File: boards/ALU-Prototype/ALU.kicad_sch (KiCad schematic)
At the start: 10 parts

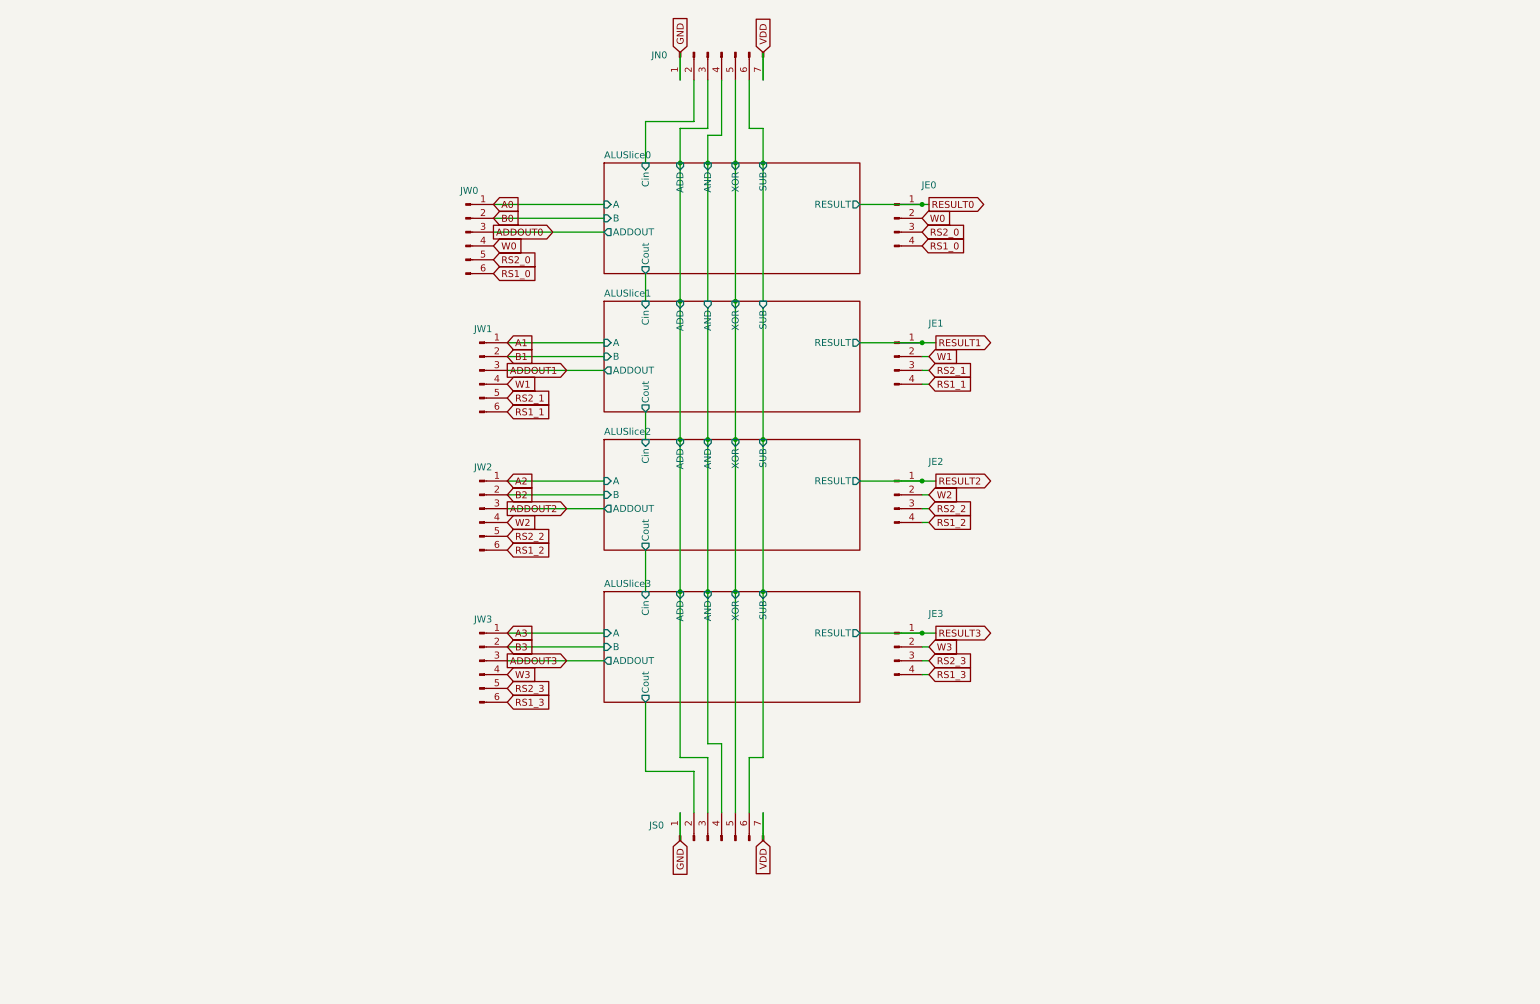
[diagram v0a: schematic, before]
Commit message: pin headers (2*17 and 2*8)
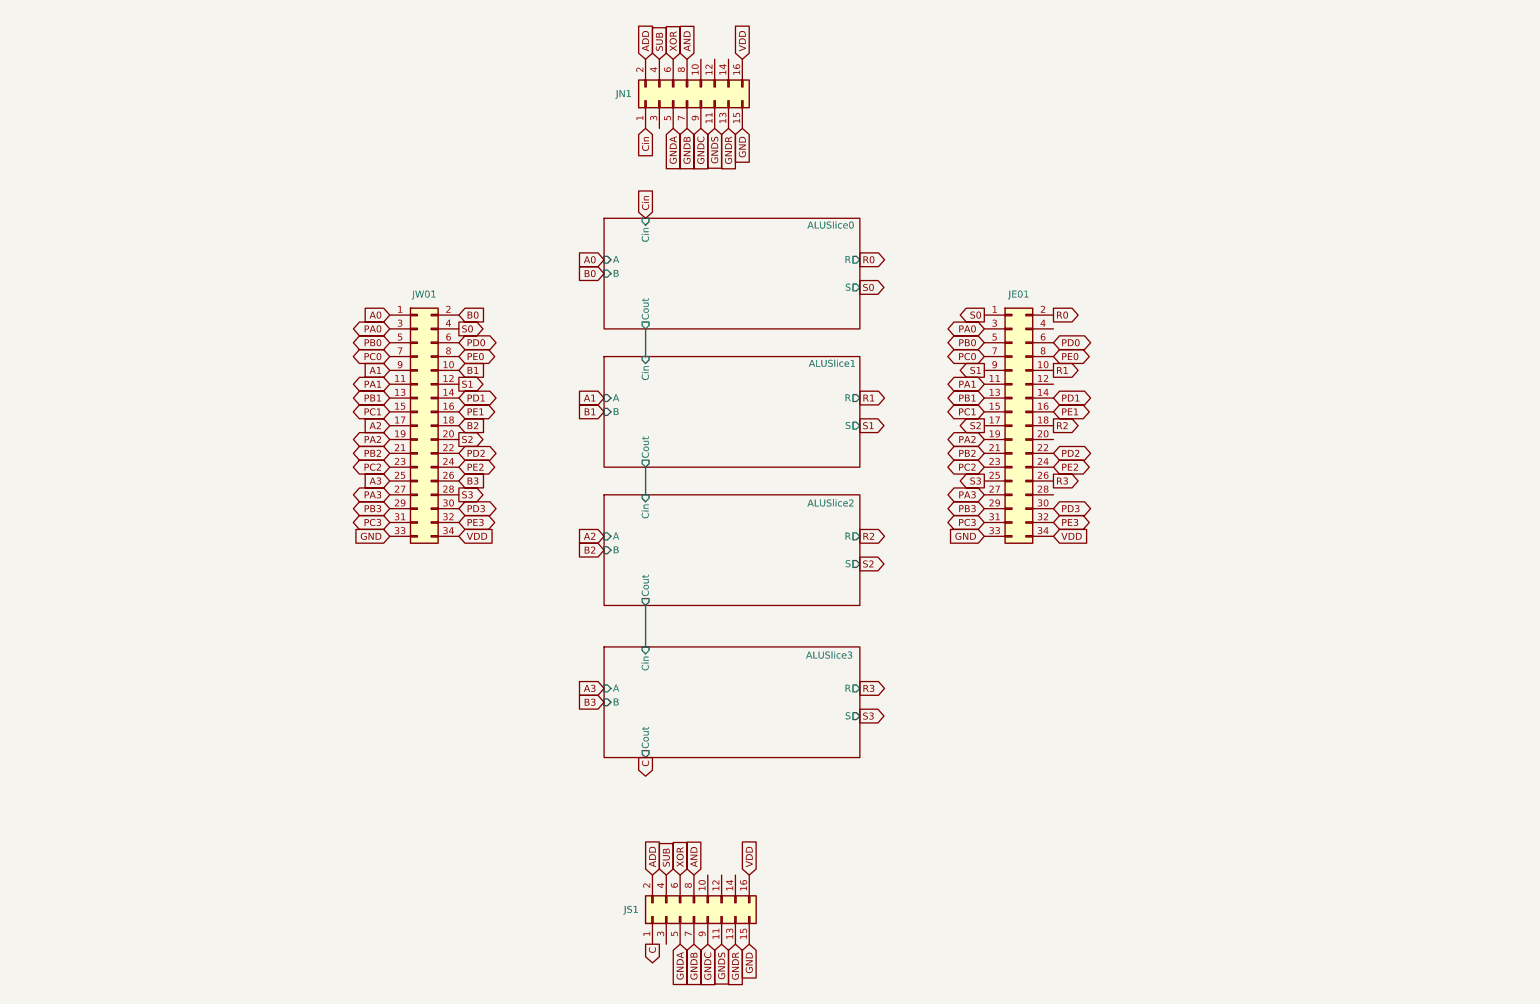
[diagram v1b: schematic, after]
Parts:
- removed JE0, JE1, JE2, JE3: Conn_01x04_Pin, Connector_PinHeader_1.27mm:PinHeader_1x04_P1.27mm_Vertical, symbol Connector:Conn_01x04_Pin
- removed JN0, JS0: Conn_01x07_Pin, Connector_PinHeader_1.27mm:PinHeader_1x07_P1.27mm_Vertical, symbol Connector:Conn_01x07_Pin
- removed JW0, JW1, JW2, JW3: Conn_01x06_Pin, Connector_PinHeader_1.27mm:PinHeader_1x06_P1.27mm_Vertical, symbol Connector:Conn_01x06_Pin
- added JE01, JW01: Conn_02x17_Odd_Even, Connector_PinHeader_2.54mm:PinHeader_2x17_P2.54mm_Vertical, symbol Connector_Generic:Conn_02x17_Odd_Even
- added JN1, JS1: Conn_02x08_Odd_Even, Connector_PinHeader_2.54mm:PinHeader_2x08_P2.54mm_Vertical, symbol Connector_Generic:Conn_02x08_Odd_Even
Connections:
- net A0: now also JW01.1 (Pin_1)
- net A1: now also JW01.9 (Pin_9)
- net A2: now also JW01.17 (Pin_17)
- net A3: now also JW01.25 (Pin_25)
- net B0: now also JW01.2 (Pin_2)
- net B1: now also JW01.10 (Pin_10)
- net B2: now also JW01.18 (Pin_18)
- net B3: now also JW01.26 (Pin_26)
- net GND: now also JE01.33 (Pin_33), JN1.15 (Pin_15), JS1.15 (Pin_15), JW01.33 (Pin_33)
- net VDD: now also JE01.34 (Pin_34), JN1.16 (Pin_16), JS1.16 (Pin_16), JW01.34 (Pin_34)
- new net ADD: JN1.2 (Pin_2), JS1.2 (Pin_2)
- new net AND: JN1.8 (Pin_8), JS1.8 (Pin_8)
- new net C: JS1.1 (Pin_1)
- new net Cin: JN1.1 (Pin_1)
- new net GNDA: JN1.5 (Pin_5), JS1.5 (Pin_5)
- new net GNDB: JN1.7 (Pin_7), JS1.7 (Pin_7)
- new net GNDC: JN1.9 (Pin_9), JS1.9 (Pin_9)
- new net GNDR: JN1.13 (Pin_13), JS1.13 (Pin_13)
- new net GNDS: JN1.11 (Pin_11), JS1.11 (Pin_11)
- new net PA0: JE01.3 (Pin_3), JW01.3 (Pin_3)
- new net PA1: JE01.11 (Pin_11), JW01.11 (Pin_11)
- new net PA2: JE01.19 (Pin_19), JW01.19 (Pin_19)
- new net PA3: JE01.27 (Pin_27), JW01.27 (Pin_27)
- new net PB0: JE01.5 (Pin_5), JW01.5 (Pin_5)
- new net PB1: JE01.13 (Pin_13), JW01.13 (Pin_13)
- new net PB2: JE01.21 (Pin_21), JW01.21 (Pin_21)
- new net PB3: JE01.29 (Pin_29), JW01.29 (Pin_29)
- new net PC0: JE01.7 (Pin_7), JW01.7 (Pin_7)
- new net PC1: JE01.15 (Pin_15), JW01.15 (Pin_15)
- new net PC2: JE01.23 (Pin_23), JW01.23 (Pin_23)
- new net PC3: JE01.31 (Pin_31), JW01.31 (Pin_31)
- new net PD0: JE01.6 (Pin_6), JW01.6 (Pin_6)
- new net PD1: JE01.14 (Pin_14), JW01.14 (Pin_14)
- new net PD2: JE01.22 (Pin_22), JW01.22 (Pin_22)
- new net PD3: JE01.30 (Pin_30), JW01.30 (Pin_30)
- new net PE0: JE01.8 (Pin_8), JW01.8 (Pin_8)
- new net PE1: JE01.16 (Pin_16), JW01.16 (Pin_16)
- new net PE2: JE01.24 (Pin_24), JW01.24 (Pin_24)
- new net PE3: JE01.32 (Pin_32), JW01.32 (Pin_32)
- new net R0: JE01.2 (Pin_2)
- new net R1: JE01.10 (Pin_10)
- new net R2: JE01.18 (Pin_18)
- new net R3: JE01.26 (Pin_26)
- new net S0: JE01.1 (Pin_1), JW01.4 (Pin_4)
- new net S1: JE01.9 (Pin_9), JW01.12 (Pin_12)
- new net S2: JE01.17 (Pin_17), JW01.20 (Pin_20)
- new net S3: JE01.25 (Pin_25), JW01.28 (Pin_28)
- new net SUB: JN1.4 (Pin_4), JS1.4 (Pin_4)
- new net XOR: JN1.6 (Pin_6), JS1.6 (Pin_6)
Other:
- sheet ALUSlice0 ports: added R, S; removed ADD, ADDOUT, AND, RESULT, SUB, XOR
- sheet ALUSlice1 ports: added R, S; removed ADD, ADDOUT, AND, RESULT, SUB, XOR
- sheet ALUSlice2 ports: added R, S; removed ADD, ADDOUT, AND, RESULT, SUB, XOR
- sheet ALUSlice3 ports: added R, S; removed ADD, ADDOUT, AND, RESULT, SUB, XOR

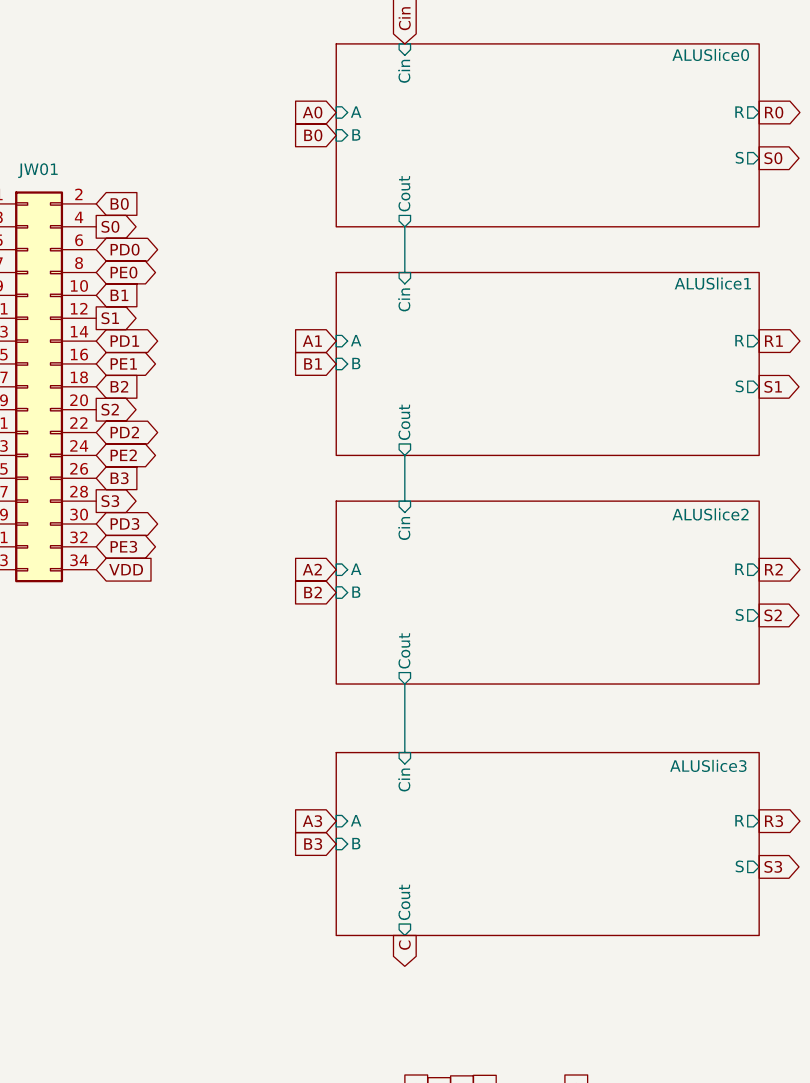
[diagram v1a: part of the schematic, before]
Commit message: Routing complete. Corrected some errors
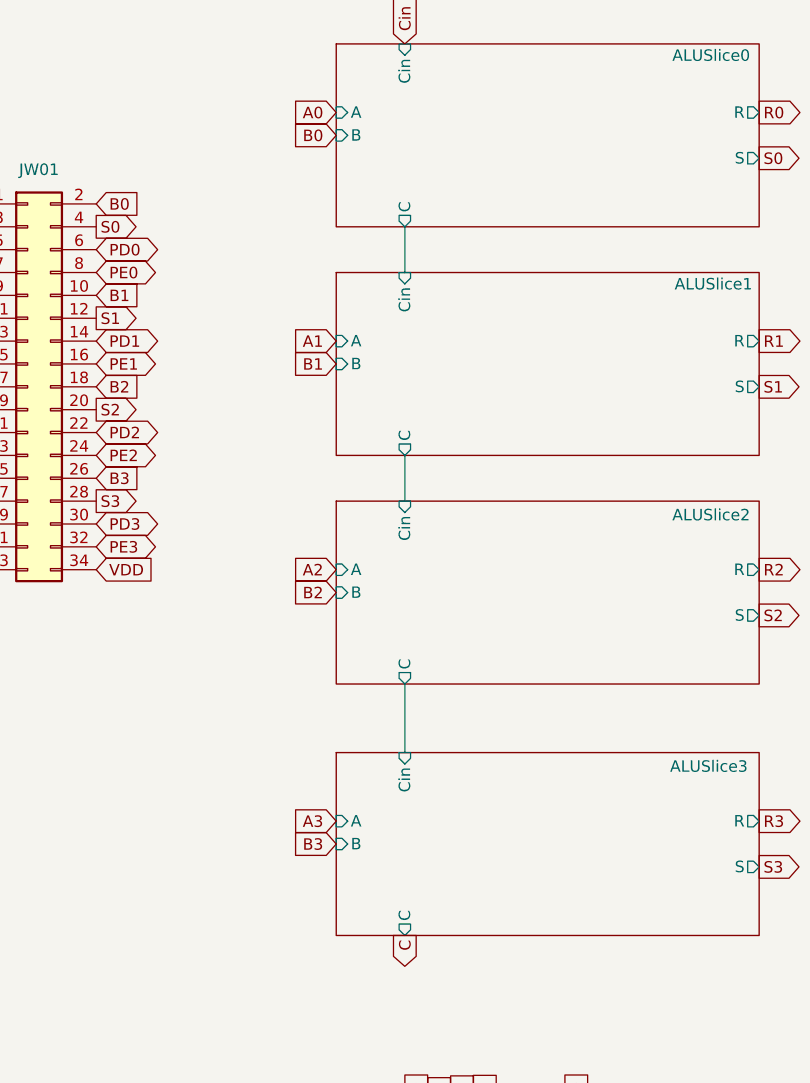
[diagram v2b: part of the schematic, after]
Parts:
- JE01, JW01: value Conn_02x17_Odd_Even -> ~
- JN1, JS1: value Conn_02x08_Odd_Even -> ~
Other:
- sheet ALUSlice0 ports: added C; removed Cout
- sheet ALUSlice1 ports: added C; removed Cout
- sheet ALUSlice2 ports: added C; removed Cout
- sheet ALUSlice3 ports: added C; removed Cout
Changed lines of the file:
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@@
 			)
 		)
-		(property "Value" "Conn_02x17_Odd_Even"
+		(property "Value" "~"
 			(at 87.63 63.5 0)
 			(effects
@@
 		)
 		(property "Description" "Generic connector, double row, 02x17, odd/even pin numbering scheme (row 1 odd numbers, row 2 even numbers), script generated (kicad-library-utils/schlib/autogen/connector/)"
+			(at 86.36 87.63 0)
+			(effects
+				(font
+					(size 1.27 1.27)
+				)
+				(hide yes)
+			)
+		)
+		(property "LCSC" ""
 			(at 86.36 87.63 0)
 			(effects
@@
 			)
 		)
-		(property "Value" "Conn_02x08_Odd_Even"
+		(property "Value" "~"
 			(at 125.73 27.9399 90)
 			(effects
@@
 		(property "Description" "Generic connector, double row, 02x08, odd/even pin numbering scheme (row 1 odd numbers, row 2 even numbers), script generated (kicad-library-utils/schlib/autogen/connector/)"
 			(at 135.89 27.94 0)
+			(effects
+				(font
+					(size 1.27 1.27)
+				)
+				(hide yes)
+			)
+		)
+		(property "LCSC" ""
+			(at 135.89 27.94 90)
 			(effects
 				(font
@@
 			)
 		)
-		(property "Value" "Conn_02x08_Odd_Even"
+		(property "Value" "~"
 			(at 127 177.7999 90)
 			(effects
@@
 		(property "Description" "Generic connector, double row, 02x08, odd/even pin numbering scheme (row 1 odd numbers, row 2 even numbers), script generated (kicad-library-utils/schlib/autogen/connector/)"
 			(at 137.16 177.8 0)
+			(effects
+				(font
+					(size 1.27 1.27)
+				)
+				(hide yes)
+			)
+		)
+		(property "LCSC" ""
+			(at 137.16 177.8 90)
 			(effects
 				(font
@@
 			)
 		)
-		(property "Value" "Conn_02x17_Odd_Even"
+		(property "Value" "~"
 			(at 196.85 63.5 0)
 			(effects
@@
 		)
 		(property "Description" "Generic connector, double row, 02x17, odd/even pin numbering scheme (row 1 odd numbers, row 2 even numbers), script generated (kicad-library-utils/schlib/autogen/connector/)"
+			(at 195.58 87.63 0)
+			(effects
+				(font
+					(size 1.27 1.27)
+				)
+				(hide yes)
+			)
+		)
+		(property "LCSC" ""
 			(at 195.58 87.63 0)
 			(effects
@@
 			)
 		)
-		(pin "Cout" output
+		(pin "C" output
 			(at 128.27 148.59 270)
 			(effects
@@
 			)
 		)
-		(pin "Cout" output
+		(pin "C" output
 			(at 128.27 120.65 270)
 			(effects
@@
 			)
 		)
-		(pin "Cout" output
+		(pin "C" output
 			(at 128.27 69.85 270)
 			(effects
@@
 			)
 		)
-		(pin "Cout" output
+		(pin "C" output
 			(at 128.27 95.25 270)
 			(effects

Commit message: First try of complete files to JLPCB
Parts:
- JE01, JN1, JS1, JW01: now left out of the parts list
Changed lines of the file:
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@@
 		(unit 1)
 		(exclude_from_sim no)
-		(in_bom yes)
+		(in_bom no)
 		(on_board yes)
 		(dnp no)
@@
 		(unit 1)
 		(exclude_from_sim no)
-		(in_bom yes)
+		(in_bom no)
 		(on_board yes)
 		(dnp no)
@@
 		(unit 1)
 		(exclude_from_sim no)
-		(in_bom yes)
+		(in_bom no)
 		(on_board yes)
 		(dnp no)
@@
 		(unit 1)
 		(exclude_from_sim no)
-		(in_bom yes)
+		(in_bom no)
 		(on_board yes)
 		(dnp no)
